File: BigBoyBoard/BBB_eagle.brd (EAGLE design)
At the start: 94 x 87.1 mm, 0 parts

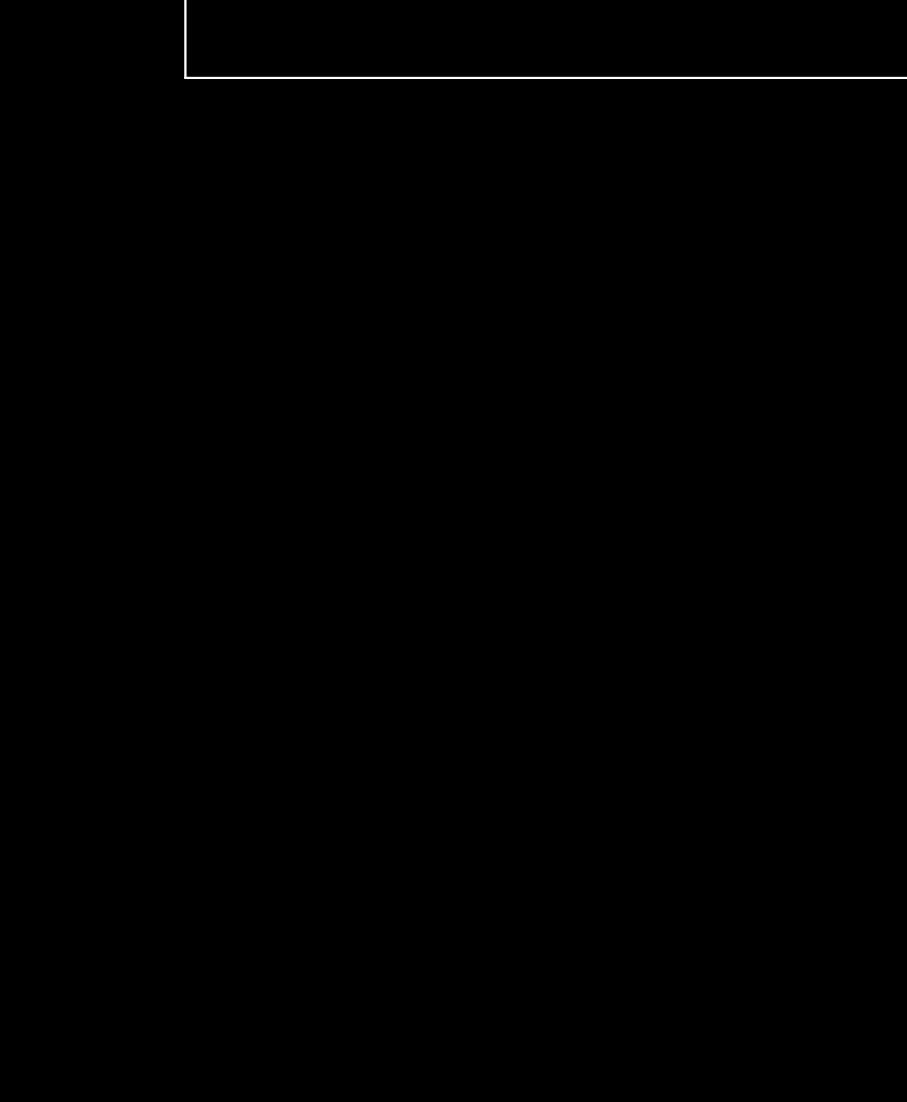
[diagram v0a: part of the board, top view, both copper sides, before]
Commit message: created prelim part layout on board
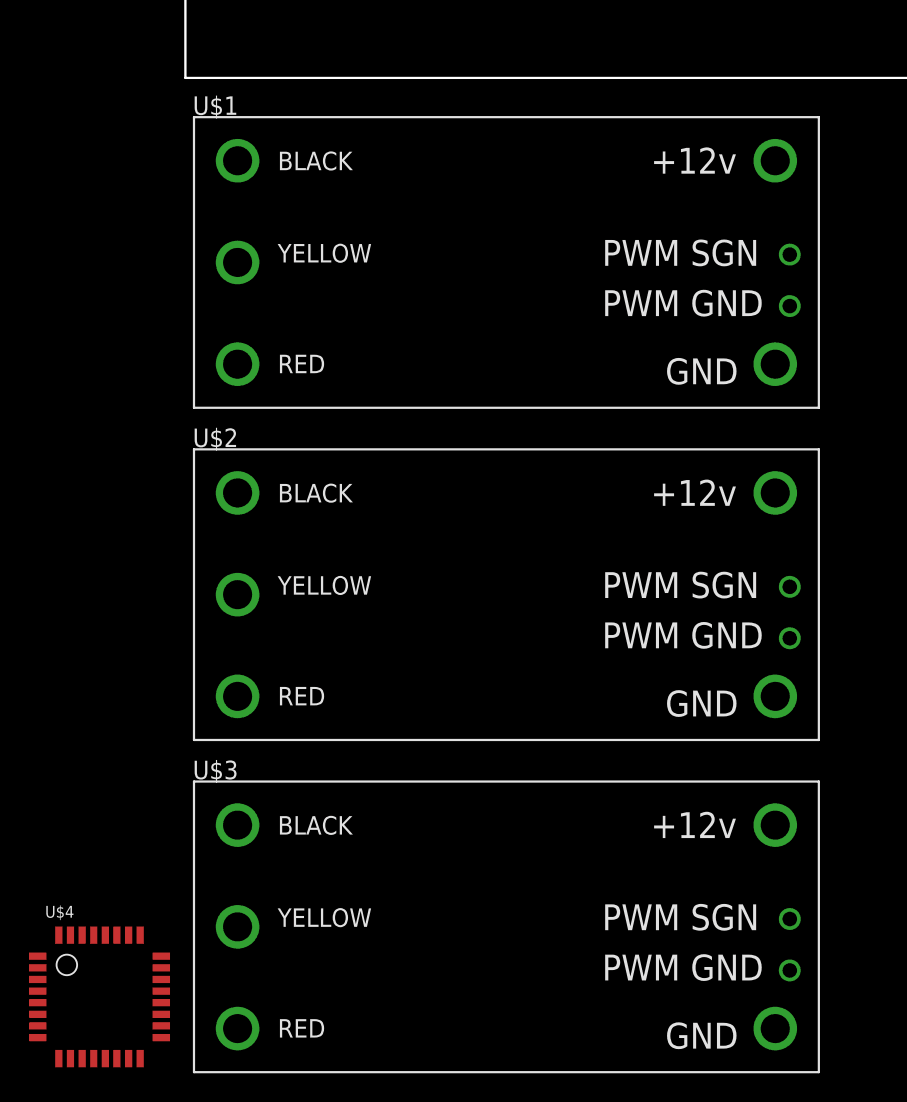
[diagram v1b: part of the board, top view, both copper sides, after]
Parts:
- added U$1, U$2, U$3: AFRO_20A_ESC, afro_20A_esc:AFRO_20A_ESC
- added U$4: STM32F042K6T6, PI_Shield_Library:STM32F042K6T6
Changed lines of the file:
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@@
 </autorouter>
 <elements>
+<element name="U$1" library="afro_20A_esc" package="AFRO_20A_ESC" value="AFRO_20A_ESC" x="21.59" y="-12.7"/>
+<element name="U$2" library="afro_20A_esc" package="AFRO_20A_ESC" value="AFRO_20A_ESC" x="21.59" y="-35.56"/>
+<element name="U$3" library="afro_20A_esc" package="AFRO_20A_ESC" value="AFRO_20A_ESC" x="21.59" y="-58.42"/>
+<element name="U$4" library="PI_Shield_Library" package="STM32F042K6T6" value="STM32F042K6T6" x="-10.16" y="-66.04"/>
 </elements>
 <signals>

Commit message: Design review 12/1
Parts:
- added C10, C11: 4.7uF, SparkFun-Capacitors:0603
- added C12, C13, C16, C7: 100nF, SparkFun-Capacitors:0603
- added C14: 0.01uf, SparkFun-Capacitors:0603
- added C15, C99: 1uF, SparkFun-Capacitors:0603
- added C17, C18: 18pF, SparkFun-Capacitors:0603
- added C5: 4.7nF, SparkFun-Capacitors:0603
- added LED1: (no value), led:CHIP-LED0805
- added R0: 0Ω, rcl:R0603
- added R1: 1KΩ, rcl:R0603
- added R10, R11: 60, SparkFun-Resistors:0603
- added R4, R6: 0, SparkFun-Resistors:0603
- added R5: 47k, SparkFun-Resistors:0603
- added RESET1: (no value), DiscreteComponents:SW_2512
- added RSH1, RSH2, RSH3, RSH7: 1 mΩ, INA4181A4:CSS2H-2512
- added SV2: (no value), con-lsta:FE05-1
- added U$14: INA4181A4, INA4181A4:SOP65P640X120-20
- added U$5: STM32F042K6T6, PI_Shield_Library:STM32F042K6T6
- added U$6: ET60T_2, ET60T:ET60T_2
- added U$7: AFRO_20A_ESC, afro_20A_esc:AFRO_20A_ESC
- added U$8: TCAN337D, PI_Shield_Library:TCAN337D
- added Y2: ECS-80-S-4X, ECS-80-S-4X:XTAL_ECS-80-S-4X
- U$4: value STM32F042K6T6 -> ET60T_1; device PI_Shield_Library:STM32F042K6T6 -> ET60T:ET60T_1
- moved U$3 116.5 mm to (71.1, 47.0)
- moved U$4 92.6 mm to (47.0, 6.74)
- moved U$2 82.6 mm to (21.6, 47.0)
- moved U$1 60.5 mm to (68.5, 25.5)
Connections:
- new net +12V: RSH1.2, RSH2.2, RSH3.2, RSH7.2, U$14.15, U$14.17, U$14.4, U$14.6, U$4.B15, U$4.B16, U$4.B7, U$4.B8, U$6.R1-1, U$6.R1-10, U$6.R1-2, U$6.R1-3, U$6.R1-4, U$6.R1-5, U$6.R1-6, U$6.R1-7, U$6.R1-8, U$6.R1-9
- new net +3V3: C10.1, C11.1, C12.1, C13.1, C14.1, C15.1, C7.1, C99.1, R5.2, SV2.5, U$14.5, U$5.VDD, U$5.VDDA, U$5.VDDIO2, U$6.R5-1, U$6.R5-10, U$6.R5-2, U$6.R5-3, U$6.R5-4, U$6.R5-5, U$6.R5-6, U$6.R5-7, U$6.R5-8, U$6.R5-9, U$8.VCC
- new net +5V: U$4.B11, U$4.B12, U$4.B19, U$4.B20, U$6.R3-1, U$6.R3-10, U$6.R3-2, U$6.R3-3, U$6.R3-4, U$6.R3-5, U$6.R3-6, U$6.R3-7, U$6.R3-8, U$6.R3-9
- new net +5VGND: U$4.B10, U$4.B17, U$4.B18, U$4.B9, U$6.R4-1, U$6.R4-10, U$6.R4-2, U$6.R4-3, U$6.R4-4, U$6.R4-5, U$6.R4-6, U$6.R4-7, U$6.R4-8, U$6.R4-9
- new net ADC_IN0: U$14.19, U$5.PA0
- new net ADC_IN1: U$14.13, U$5.PA1
- new net ADC_IN2: U$14.2, U$5.PA2
- new net ADC_IN3: U$14.8, U$5.PA3
- new net CAN_H: R10.2, U$4.B24, U$8.CANH
- new net CAN_L: R11.1, U$4.B23, U$8.CANL
- new net CAN_RX: U$5.PA11, U$8.TXD
- new net CAN_TX: U$5.PA12, U$8.RXD
- new net ESC1_R1: U$1.RED, U$4.R1-1, U$4.R1-10, U$4.R1-2, U$4.R1-3, U$4.R1-4, U$4.R1-5, U$4.R1-6, U$4.R1-7, U$4.R1-8, U$4.R1-9
- new net ESC1_R2: U$1.YEL, U$4.R2-1, U$4.R2-10, U$4.R2-2, U$4.R2-3, U$4.R2-4, U$4.R2-5, U$4.R2-6, U$4.R2-7, U$4.R2-8, U$4.R2-9
- new net ESC1_R3: U$1.BLK, U$4.R3-1, U$4.R3-10, U$4.R3-2, U$4.R3-3, U$4.R3-4, U$4.R3-5, U$4.R3-6, U$4.R3-7, U$4.R3-8, U$4.R3-9
- new net ESC2_L1: U$2.RED, U$4.L1-1, U$4.L1-10, U$4.L1-2, U$4.L1-3, U$4.L1-4, U$4.L1-5, U$4.L1-6, U$4.L1-7, U$4.L1-8, U$4.L1-9
- new net ESC2_L2: U$2.YEL, U$4.L2-1, U$4.L2-10, U$4.L2-2, U$4.L2-3, U$4.L2-4, U$4.L2-5, U$4.L2-6, U$4.L2-7, U$4.L2-8, U$4.L2-9
- new net ESC2_L3: U$2.BLK, U$4.L3-1, U$4.L3-10, U$4.L3-2, U$4.L3-3, U$4.L3-4, U$4.L3-5, U$4.L3-6, U$4.L3-7, U$4.L3-8, U$4.L3-9
- new net ESC3_R4: U$3.RED, U$4.R4-1, U$4.R4-10, U$4.R4-2, U$4.R4-3, U$4.R4-4, U$4.R4-5, U$4.R4-6, U$4.R4-7, U$4.R4-8, U$4.R4-9
- new net ESC3_R5: U$3.YEL, U$4.R5-1, U$4.R5-10, U$4.R5-2, U$4.R5-3, U$4.R5-4, U$4.R5-5, U$4.R5-6, U$4.R5-7, U$4.R5-8, U$4.R5-9
- new net ESC3_R6: U$3.BLK, U$4.R6-1, U$4.R6-10, U$4.R6-2, U$4.R6-3, U$4.R6-4, U$4.R6-5, U$4.R6-6, U$4.R6-7, U$4.R6-8, U$4.R6-9
- new net ESC7_L4: U$4.L4-1, U$4.L4-10, U$4.L4-2, U$4.L4-3, U$4.L4-4, U$4.L4-5, U$4.L4-6, U$4.L4-7, U$4.L4-8, U$4.L4-9, U$7.RED
- new net ESC7_L5: U$4.L5-1, U$4.L5-10, U$4.L5-2, U$4.L5-3, U$4.L5-4, U$4.L5-5, U$4.L5-6, U$4.L5-7, U$4.L5-8, U$4.L5-9, U$7.YEL
- new net ESC7_L6: U$4.L6-1, U$4.L6-10, U$4.L6-2, U$4.L6-3, U$4.L6-4, U$4.L6-5, U$4.L6-6, U$4.L6-7, U$4.L6-8, U$4.L6-9, U$7.BLK
- new net GND: C5.1, C7.2, R0.2, U$1.GND, U$1.PWM_GND, U$2.GND, U$2.PWM_GND, U$3.GND, U$3.PWM_GND, U$4.B13, U$4.B14, U$4.B21, U$4.B22, U$6.R2-1, U$6.R2-10, U$6.R2-2, U$6.R2-3, U$6.R2-4, U$6.R2-5, U$6.R2-6, U$6.R2-7, U$6.R2-8, U$6.R2-9, U$7.GND, U$7.PWM_GND, U$8.GND
- new net GNDA: C10.2, C11.2, C12.2, C13.2, C14.2, C15.2, C16.2, C17.2, C18.2, C99.2, LED1.C, R0.1, RESET1.1, SV2.1, U$14.1, U$14.12, U$14.16, U$14.20, U$14.9, U$5.PB8-BOOT0, U$5.VSS, U$5.VSS1, U$6.R6-1, U$6.R6-10, U$6.R6-2, U$6.R6-3, U$6.R6-4, U$6.R6-5, U$6.R6-6, U$6.R6-7, U$6.R6-8, U$6.R6-9
- new net N$1: R1.1, U$5.PA15
- new net N$12: U$4.B6
- new net N$13: U$4.B5
- new net N$14: U$4.B4
- new net N$15: U$4.B3
- new net N$16: U$4.B2
- new net N$17: U$4.B1
- new net N$2: LED1.A, R1.2
- new net N$3: C18.1, R4.1, Y2.2
- new net N$30: U$6.B24
- new net N$31: U$6.B23
- new net N$32: U$6.B22
- new net N$33: U$6.B21
- new net N$34: U$6.B20
- new net N$35: U$6.B19
- new net N$36: U$6.B18
- new net N$37: U$6.B17
- new net N$38: U$6.B16
- new net N$39: U$6.B15
- new net N$4: C17.1, R6.1, Y2.1
- new net N$40: U$6.B14
- new net N$41: U$6.B13
- new net N$42: U$6.B1
- new net N$43: U$6.B2
- new net N$44: U$6.B3
- new net N$45: U$6.B4
- new net N$46: U$6.B5
- new net N$47: U$6.B6
- new net N$48: U$6.B7
- new net N$49: U$6.B8
- new net N$5: C5.2, R10.1, R11.2
- new net N$50: U$6.B9
- new net N$51: U$6.B10
- new net N$52: U$6.B11
- new net N$53: U$6.B12
- new net N$58: U$14.11
- new net NRST: C16.1, R5.1, RESET1.2, SV2.2, U$5.NRST
- new net OSC_IN: R6.2, U$5.PF0-OSC_IN
- new net OSC_OUT: R4.2, U$5.PF1-OSC_OUT
- new net SWCLK: SV2.3, U$5.PA14
- new net SWDIO: SV2.4, U$5.PA13
- new net TIM3_CH1: U$5.PA6, U$7.PWM_SGN
- new net TIM3_CH2: U$2.PWM_SGN, U$5.PA7
- new net TIM3_CH3: U$1.PWM_SGN, U$5.PB0
- new net TIM3_CH4: U$3.PWM_SGN, U$5.PB1
- new net VCC1: RSH1.1, U$1.VCC, U$14.7
- new net VCC2: RSH2.1, U$14.18, U$2.VCC
- new net VCC3: RSH3.1, U$14.3, U$3.VCC
- new net VCC7: RSH7.1, U$14.14, U$7.VCC
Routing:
- net +12V: track 0.00 -> 238.9 mm, vias 0 -> 13
- net +3V3: track 0.00 -> 219.0 mm, vias 0 -> 8
- net +5VGND: track 0.00 -> 209.8 mm, vias 0 -> 1
- net GNDA: track 0.00 -> 208.4 mm, vias 0 -> 6
- net +5V: track 0.00 -> 207.4 mm, vias 0 -> 1
- net CAN_L: track 0.00 -> 106.3 mm, vias 0 -> 2
- net CAN_H: track 0.00 -> 99.9 mm
- net TIM3_CH3: track 0.00 -> 84.9 mm, vias 0 -> 2
- net TIM3_CH4: track 0.00 -> 74.9 mm, vias 0 -> 1
- net VCC3: track 0.00 -> 72.6 mm, vias 0 -> 3
- net VCC1: track 0.00 -> 66.2 mm, vias 0 -> 1
- net GND: track 0.00 -> 56.5 mm, vias 0 -> 1
- net CAN_RX: track 0.00 -> 49.7 mm, vias 0 -> 2
- net NRST: track 0.00 -> 47.9 mm, vias 0 -> 2
- net CAN_TX: track 0.00 -> 41.8 mm, vias 0 -> 2
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- added copper zone on layer 1, net +12V
- added copper zone on layer 16, net +12V
- added copper zone on layer 1, net ESC1_R1
- added copper zone on layer 1, net ESC1_R2
- added copper zone on layer 1, net ESC1_R3
- added copper zone on layer 16, net ESC2_L1
- added copper zone on layer 16, net ESC2_L2
- added copper zone on layer 16, net ESC2_L3
- added copper zone on layer 16, net ESC3_R4
- added copper zone on layer 16, net ESC3_R5
- added copper zone on layer 16, net ESC3_R6
- added copper zone on layer 1, net ESC7_L4
- added copper zone on layer 1, net ESC7_L5
- added copper zone on layer 1, net ESC7_L6
- added copper zone on layer 1, net GND
- added copper zone on layer 16, net GND
- added copper zone on layer 1, net VCC1
- added copper zone on layer 16, net VCC2
- added copper zone on layer 1, net VCC3
- added copper zone on layer 16, net VCC7

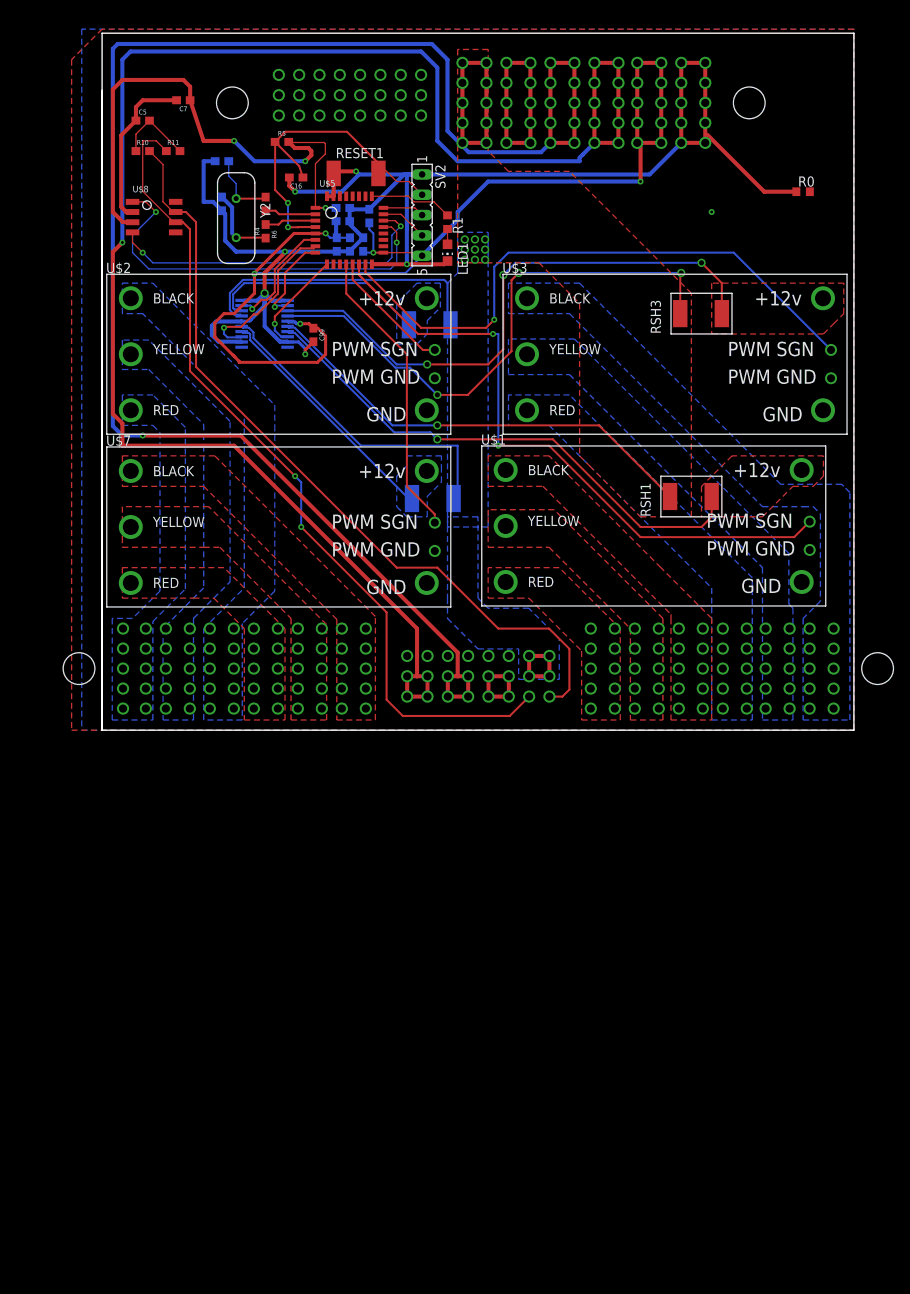
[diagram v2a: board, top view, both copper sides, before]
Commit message: Tenatively compleated esc board
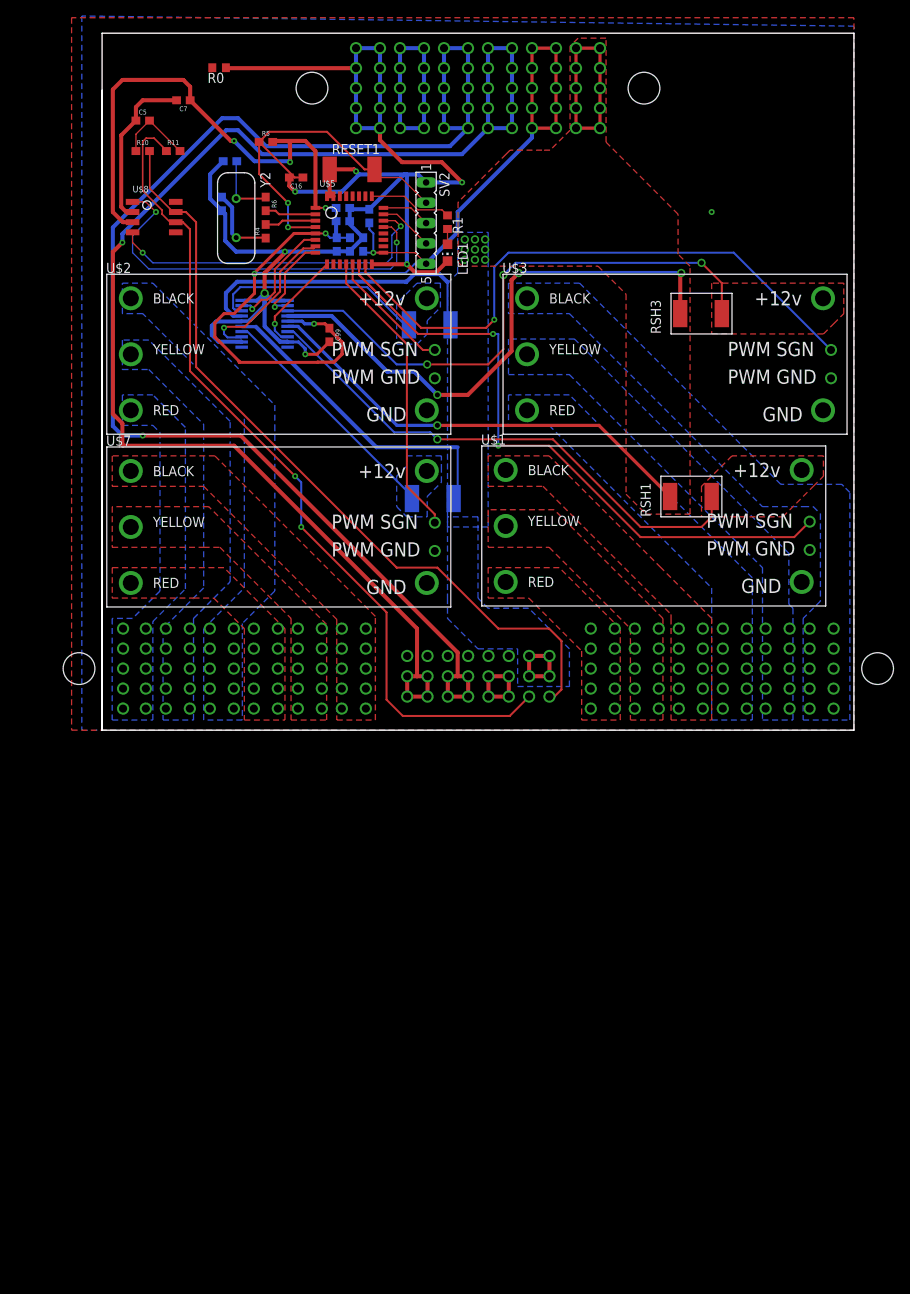
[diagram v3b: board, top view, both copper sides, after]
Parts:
- moved R0 74.6 mm to (14.6, 82.8), turned to 180 degrees
- moved U$6 16.0 mm to (47.0, 80.3)
- moved C99 2.00 mm to (28.4, 49.4)
- moved R5 2.00 mm to (20.5, 73.5)
- moved SV2 1.12 mm to (40.5, 63.4)
- moved C17 1.00 mm to (16.0, 71.1)
- moved RESET1 0.71 mm to (31.2, 70.1)
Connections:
- removed net N$30: U$6.B24
- removed net N$31: U$6.B23
- removed net N$32: U$6.B22
- removed net N$33: U$6.B21
- removed net N$34: U$6.B20
- removed net N$35: U$6.B19
- removed net N$36: U$6.B18
- removed net N$37: U$6.B17
- removed net N$38: U$6.B16
- removed net N$39: U$6.B15
- removed net N$40: U$6.B14
- removed net N$41: U$6.B13
- removed net N$42: U$6.B1
- removed net N$43: U$6.B2
- removed net N$44: U$6.B3
- removed net N$45: U$6.B4
- removed net N$46: U$6.B5
- removed net N$47: U$6.B6
- removed net N$48: U$6.B7
- removed net N$49: U$6.B8
- removed net N$50: U$6.B9
- removed net N$51: U$6.B10
- removed net N$52: U$6.B11
- removed net N$53: U$6.B12
- net +12V: now also U$6.R6-1, U$6.R6-10, U$6.R6-2, U$6.R6-3, U$6.R6-4, U$6.R6-5, U$6.R6-6, U$6.R6-7, U$6.R6-8, U$6.R6-9; no longer U$6.R1-1, U$6.R1-10, U$6.R1-2, U$6.R1-3, U$6.R1-4, U$6.R1-5, U$6.R1-6, U$6.R1-7, U$6.R1-8, U$6.R1-9
- net GNDA: now also U$6.R1-1, U$6.R1-10, U$6.R1-2, U$6.R1-3, U$6.R1-4, U$6.R1-5, U$6.R1-6, U$6.R1-7, U$6.R1-8, U$6.R1-9; no longer U$6.R6-1, U$6.R6-10, U$6.R6-2, U$6.R6-3, U$6.R6-4, U$6.R6-5, U$6.R6-6, U$6.R6-7, U$6.R6-8, U$6.R6-9
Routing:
- net +5VGND: track 209.8 -> 169.5 mm
- net +5V: track 207.4 -> 171.2 mm
- net +3V3: track 219.0 -> 205.4 mm, vias 8 -> 7
- net GNDA: track 208.4 -> 195.6 mm, vias 6 -> 7
- net CAN_L: track 106.3 -> 108.3 mm
- net CAN_H: track 99.9 -> 98.1 mm
- net +12V: track 238.9 -> 240.1 mm
- net SWDIO: track 5.93 -> 6.84 mm
- net SWCLK: track 5.21 -> 6.12 mm

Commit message: Continued work on ESC board for review
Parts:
- moved C16 1.00 mm to (23.3, 69.1), turned to 0 degrees
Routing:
- net GND: track 56.5 -> 137.2 mm, vias 1 -> 7
- net CAN_H: track 98.1 -> 96.1 mm
- net NRST: track 47.8 -> 46.1 mm
- net +3V3: track 205.4 -> 204.3 mm
- net GNDA: track 195.6 -> 196.5 mm
